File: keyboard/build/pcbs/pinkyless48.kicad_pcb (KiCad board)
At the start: 2 copper layers, 136.1 x 162.6 mm, 49 parts

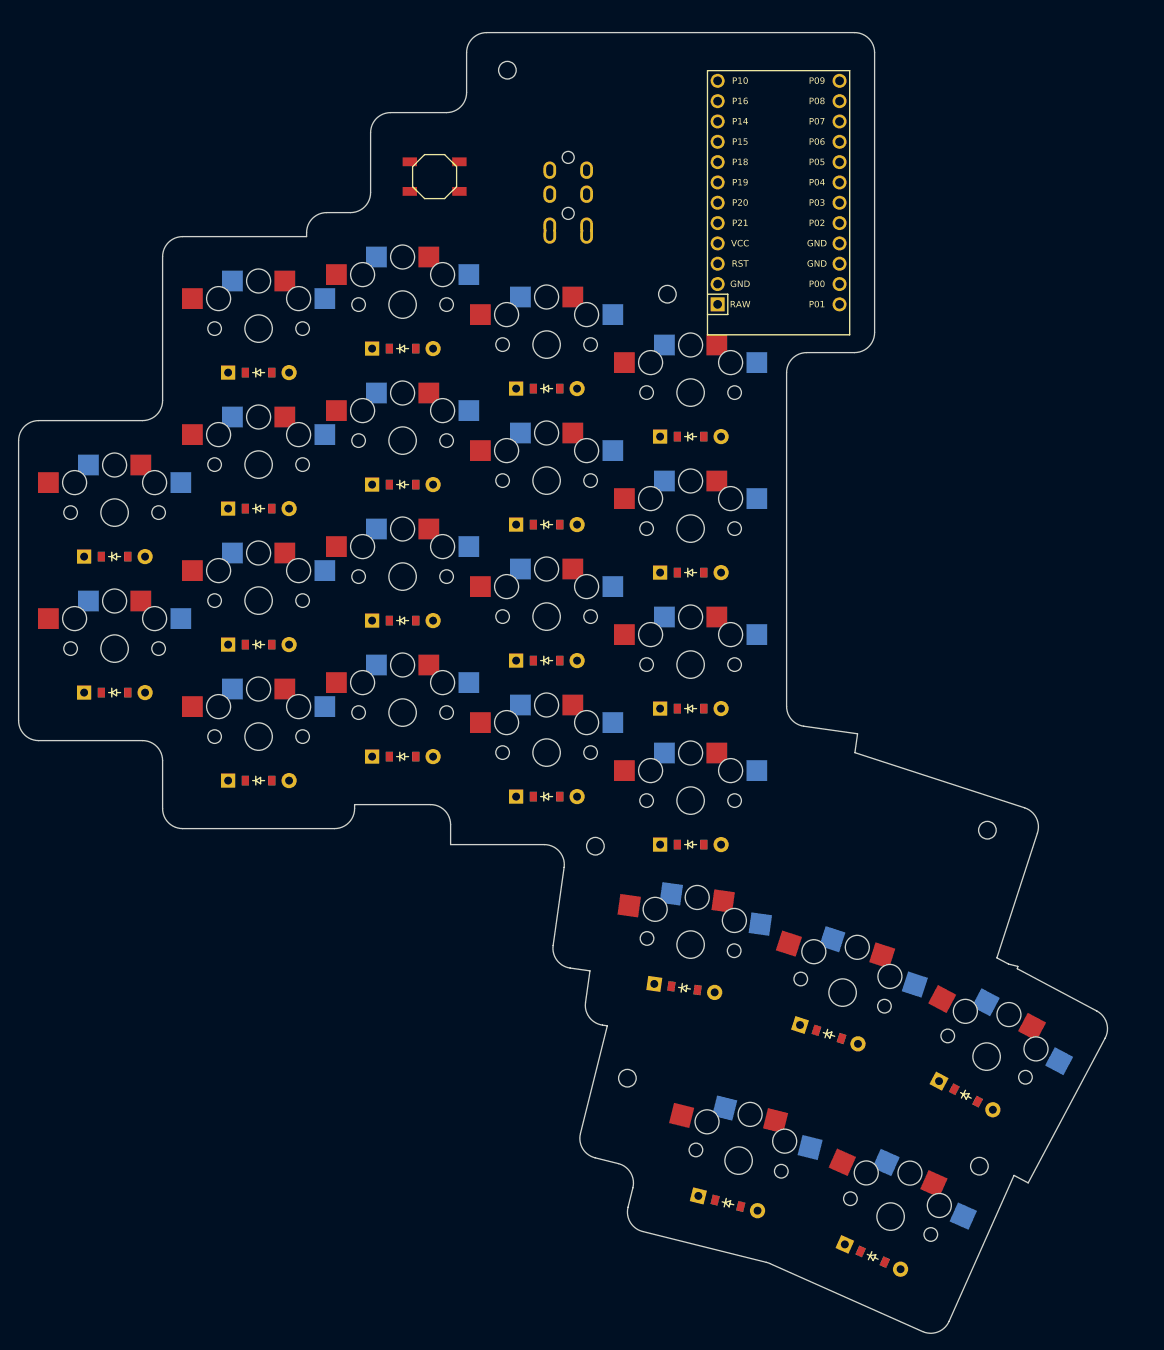
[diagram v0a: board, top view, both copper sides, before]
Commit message: Add pinky number key, flatten stagger, tighten board outline
Three changes, renaming the board to pinkyless48.

Pinky gains a third key. It now drops only the bottom row, keeping number,
top and home. With all five columns present the number row carries a full
1234567890 across the two halves, so digits no longer need a layer. 24 keys
per half, 24 of 25 matrix cells used.

Column stagger reworked to a flat profile: inner, index and ring level with
each other, middle 4 mm forward, pinky 6 mm back. This is not the usual
finger-length stagger.

That change exposed a real constraint. The reversible Choc hotswap footprint
carries socket pads for BOTH faces and is +/-9.58 mm wide, so two columns at
the same height short against each other at an 18 mm pitch - index and inner
are now level and overlapped by 2.99 mm^2. Clearing it needs either 19.4 mm
of pitch or 2.9 mm of vertical offset. Rather than widen every column, only
the inner column's pitch opens to 19.8 mm; every other gap stays at 18 mm and
clears on vertical offset alone. Tightest different-net gap is now 0.650 mm.

Board outline tightened. The two large bridge rectangles are gone: they dated
from when the thumb cluster sat far below the matrix, and now that it starts
at the inner column its key pads already overlap their neighbours. A single
small web patch covers the one gap the thumb keys leave between them. The
reset button moves in beside the controller instead of sitting far outboard,
and the jack pad narrows from 30 to 16 mm, removing the wide slab of empty
board across the top.

Also fixes a genuine bug in find_mounts.py: the reference anchor was
hardcoded at matrix_pinky_home's old coordinates, so once the stagger moved
that key every emitted screw position was offset by 6 mm. It now reads the
anchor from the build.

Case STLs, QMK keyboard.json and the keymap regenerated for 48 keys. All five
checks pass.

Co-Authored-By: Claude Opus 5 <noreply@anthropic.com>
Claude-Session: https://claude.ai/code/sess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
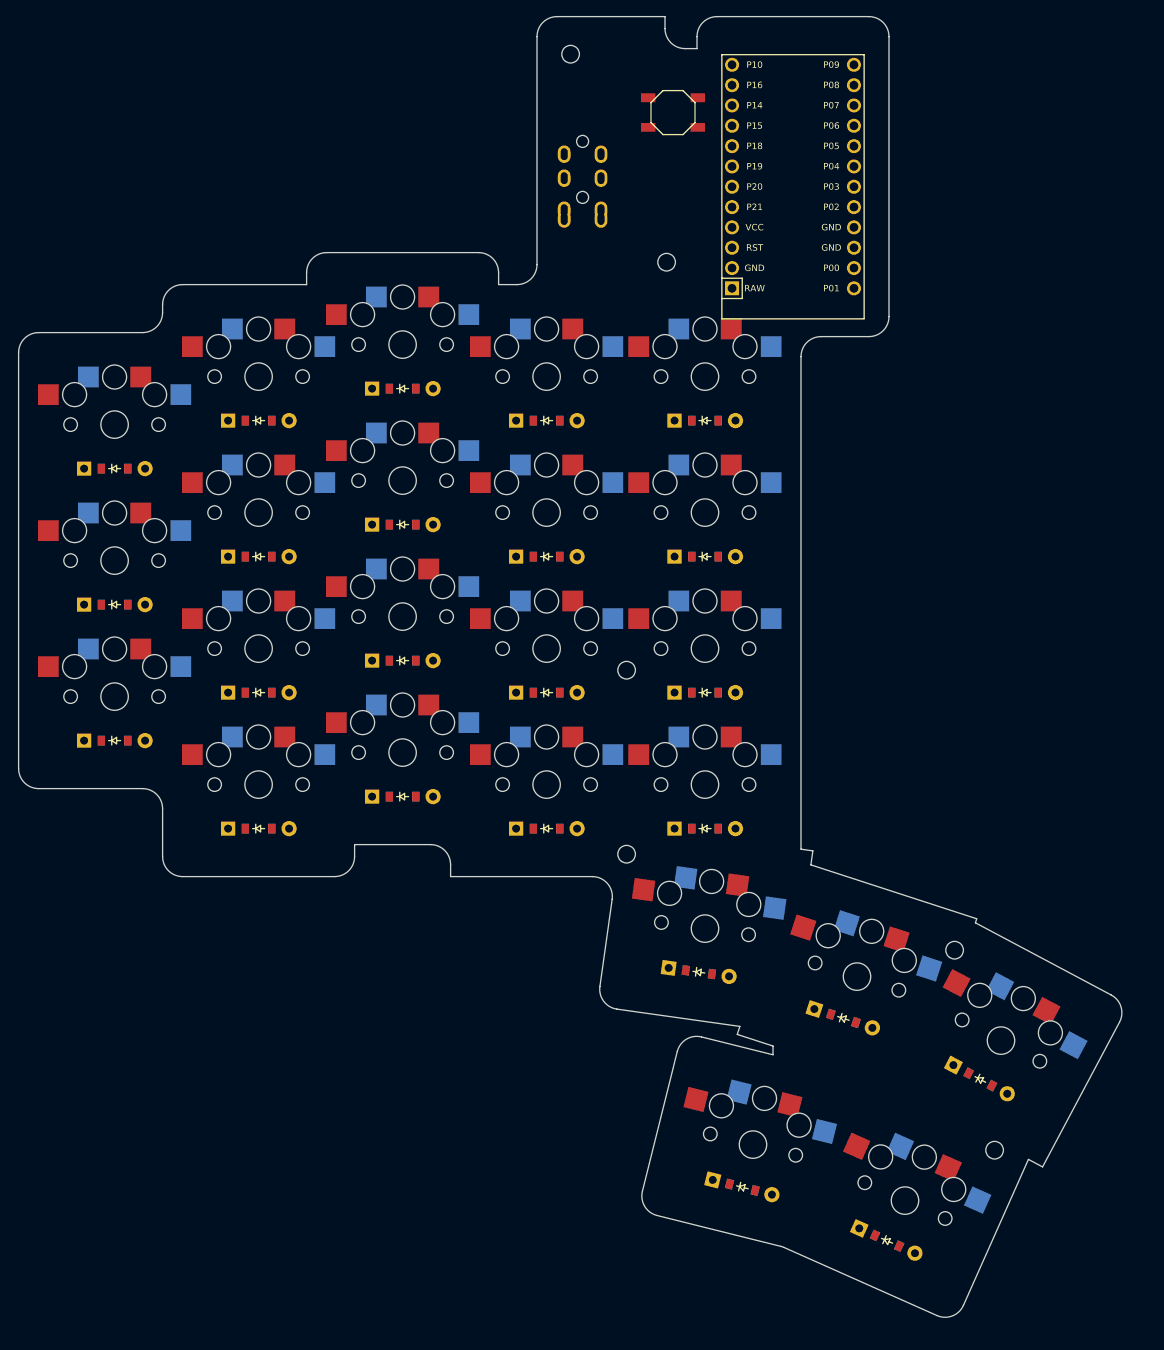
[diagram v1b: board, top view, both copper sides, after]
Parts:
- added D24: , ComboDiode, F.Cu at (156.6, 217.0)
- added S24: , PG1350, F.Cu at (158.8, 212.0)
- moved S19 71.0 mm to (133.8, 109.0), turned to 0 degrees
- moved D19 71.0 mm to (133.8, 114.5), turned to 0 degrees
- moved D15 56.0 mm to (114.0, 114.5)
- moved S15 56.0 mm to (114.0, 109.0)
- moved D11 54.1 mm to (96.0, 110.5)
- moved S11 54.1 mm to (96.0, 105.0)
- moved D7 45.7 mm to (78.0, 114.5)
- moved S7 45.7 mm to (78.0, 109.0)
- moved D3 43.0 mm to (60.0, 120.5)
- moved S3 43.0 mm to (60.0, 115.0)
- moved S22 36.1 mm to (170.8, 192.0), turned to -28 degrees
- moved D22 35.1 mm to (168.2, 196.9), turned to -28 degrees
- moved B1 30.9 mm to (129.8, 76.0)
- moved D4 23.0 mm to (78.0, 165.5)
- moved D5 23.0 mm to (78.0, 148.5)
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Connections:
- D10 pad 1: R4 -> R3
- D10 pad 2: middle_num -> middle_top
- D11 pad 1: R1 -> R4
- D11 pad 2: index_bottom -> middle_num
- D12 pad 1: R2 -> R1
- D12 pad 2: index_home -> index_bottom
- D13 pad 1: R3 -> R2
- D13 pad 2: index_top -> index_home
- D14 pad 1: R4 -> R3
- D14 pad 2: index_num -> index_top
- D15 pad 1: R1 -> R4
- D15 pad 2: inner_bottom -> index_num
- D16 pad 1: R2 -> R1
- D16 pad 2: inner_home -> inner_bottom
- D17 pad 1: R3 -> R2
- D17 pad 2: inner_top -> inner_home
- D18 pad 1: R4 -> R3
- D18 pad 2: inner_num -> inner_top
- D19 pad 1: R5 -> R4
- D19 pad 2: t1_thumb -> inner_num
- D20 pad 2: t2_thumb -> t1_thumb
- D21 pad 2: t3_thumb -> t2_thumb
- D22 pad 2: t4_thumb -> t3_thumb
- D23 pad 2: t5_thumb -> t4_thumb
- D3 pad 1: R1 -> R4
- D3 pad 2: ring_bottom -> pinky_num
- D4 pad 1: R2 -> R1
- D4 pad 2: ring_home -> ring_bottom
- D5 pad 1: R3 -> R2
- D5 pad 2: ring_top -> ring_home
- D6 pad 1: R4 -> R3
- D6 pad 2: ring_num -> ring_top
- D7 pad 1: R1 -> R4
- D7 pad 2: middle_bottom -> ring_num
- D8 pad 1: R2 -> R1
- D8 pad 2: middle_home -> middle_bottom
- D9 pad 1: R3 -> R2
- D9 pad 2: middle_top -> middle_home
- S10 pad 1: middle_num -> middle_top
- S11 pad 1: index_bottom -> middle_num
- S11 pad 2: C4 -> C3
- S12 pad 1: index_home -> index_bottom
- S13 pad 1: index_top -> index_home
- S14 pad 1: index_num -> index_top
- S15 pad 1: inner_bottom -> index_num
- S15 pad 2: C5 -> C4
- S16 pad 1: inner_home -> inner_bottom
- S17 pad 1: inner_top -> inner_home
- S18 pad 1: inner_num -> inner_top
- S19 pad 1: t1_thumb -> inner_num
- S19 pad 2: C1 -> C5
- S20 pad 1: t2_thumb -> t1_thumb
- S20 pad 2: C2 -> C1
- S21 pad 1: t3_thumb -> t2_thumb
- S21 pad 2: C3 -> C2
- S22 pad 1: t4_thumb -> t3_thumb
- S22 pad 2: C4 -> C3
- S23 pad 1: t5_thumb -> t4_thumb
- S23 pad 2: C5 -> C4
- S3 pad 1: ring_bottom -> pinky_num
- S3 pad 2: C2 -> C1
- S4 pad 1: ring_home -> ring_bottom
- S5 pad 1: ring_top -> ring_home
- S6 pad 1: ring_num -> ring_top
- S7 pad 1: middle_bottom -> ring_num
- S7 pad 2: C3 -> C2
- S8 pad 1: middle_home -> middle_bottom
- S9 pad 1: middle_top -> middle_home
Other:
- board size 136.1 x 162.6 mm -> 137.9 x 162.6 mm

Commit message: Move controller into the notch beside the thumb cluster
The strip of board above the matrix was 29.5 mm tall and 41% empty. It
existed only because the controller was mounted standing on end: a Pro Micro
is 33 x 18 mm, so vertically it forced the board ~30 mm taller than the
tallest key just to clear it.

Because the thumb cluster runs inboard and down, the area outboard of it and
below the number row is dead space that already sits inside the board's
bounding box. The controller, TRRS jack and reset button now live there, laid
flat with the USB port facing inboard so the cable exits between the halves.
Filling that notch costs nothing in overall size, and the strip above the
matrix disappears entirely.

Board drops from 137.9 x 162.6 mm to 137.9 x 133.1 mm per half - 29.5 mm
shorter, an 18% smaller bounding box, which is also what JLCPCB charges by.

The three separate connector pads collapse into one pad covering the whole
controller area, since the jack and reset button now sit inside it.

Screw positions re-derived. Case STLs, QMK keyboard.json and previews
regenerated. All five checks pass; controller opening now clears the nearest
switch cutout by 3.90 mm, up from 2.05 mm.

Co-Authored-By: Claude Opus 5 <noreply@anthropic.com>
Claude-Session: https://claude.ai/code/session_01TKXtddA7pBLooPYbDwxvxo
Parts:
- moved MCU1 49.0 mm to (161.8, 130.0), turned to 180 degrees
- moved TRRS1 48.5 mm to (161.8, 104.0)
- moved B1 34.4 mm to (149.8, 104.0)
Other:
- board size 137.9 x 162.6 mm -> 137.9 x 133.1 mm

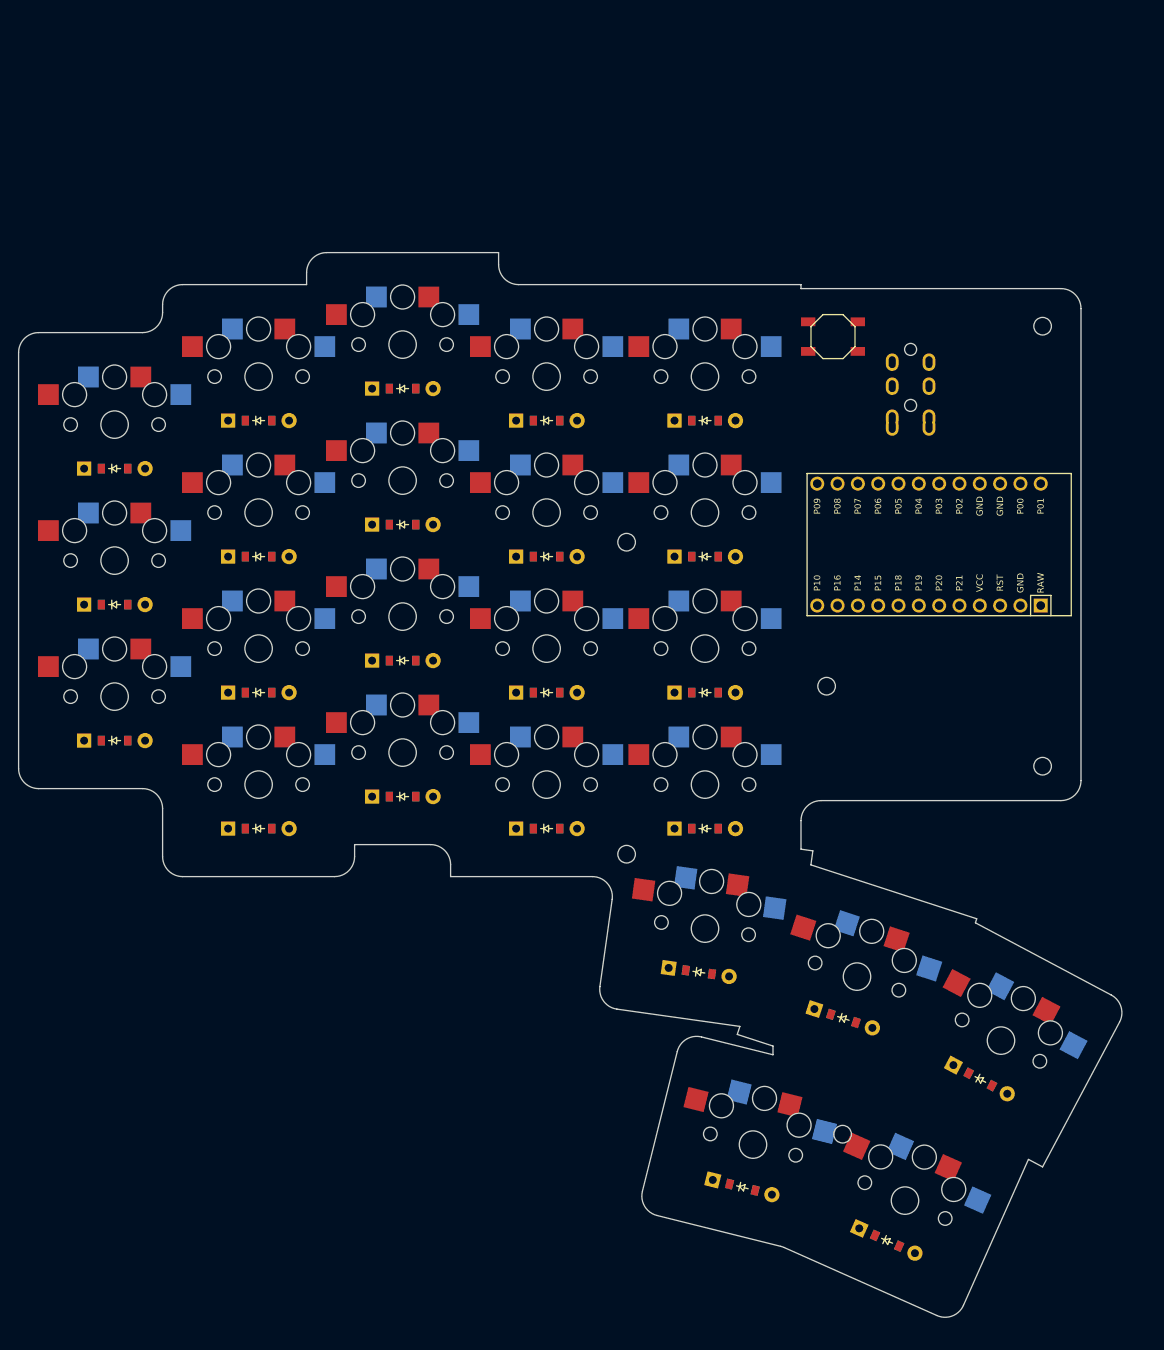
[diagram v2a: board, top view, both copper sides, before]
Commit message: Fill concave notches in the board outline
The outline had ten concave pockets where the thumb cluster, the controller
area and the grown key pads met. They are dead space, and their sharp inside
corners are crack initiation points in both 1.6 mm FR4 and the 1.3 mm printed
plate.

The outline is now morphologically closed - grown by 6 mm, then shrunk by the
same 6 mm - before filleting. That fills any pocket narrower than roughly
12 mm while leaving the board's overall L-shape alone. A convex hull was the
obvious alternative and is wrong here: it would swallow the entire empty
region outboard of the thumb cluster and add roughly 40 cm^2 of pointless
board.

Measured effect: pockets 10 -> 1 (the survivor is a 2 mm^2 sliver), board area
116.0 -> 117.7 cm^2 (+1.5%), bounding box unchanged at 137.9 x 133.1 mm.

Worth recording that the fragility concern did not hold up on measurement:
eroding the outline until it splits showed the narrowest neck was already
22.2 mm, not thin enough to snap. The closing was still worth doing for the
stress risers and the simpler plate, and it takes the neck to 33.0 mm.

check_outline.py now measures both properties on every build - narrowest neck
(fails under 8 mm) and any remaining concave pocket over 100 mm^2 - so a
future layout change cannot quietly reintroduce a fragile outline.

Case STLs, QMK keyboard.json and previews regenerated. All five checks pass.

Co-Authored-By: Claude Opus 5 <noreply@anthropic.com>
Claude-Session: https://claude.ai/code/session_01TKXtddA7pBLooPYbDwxvxo
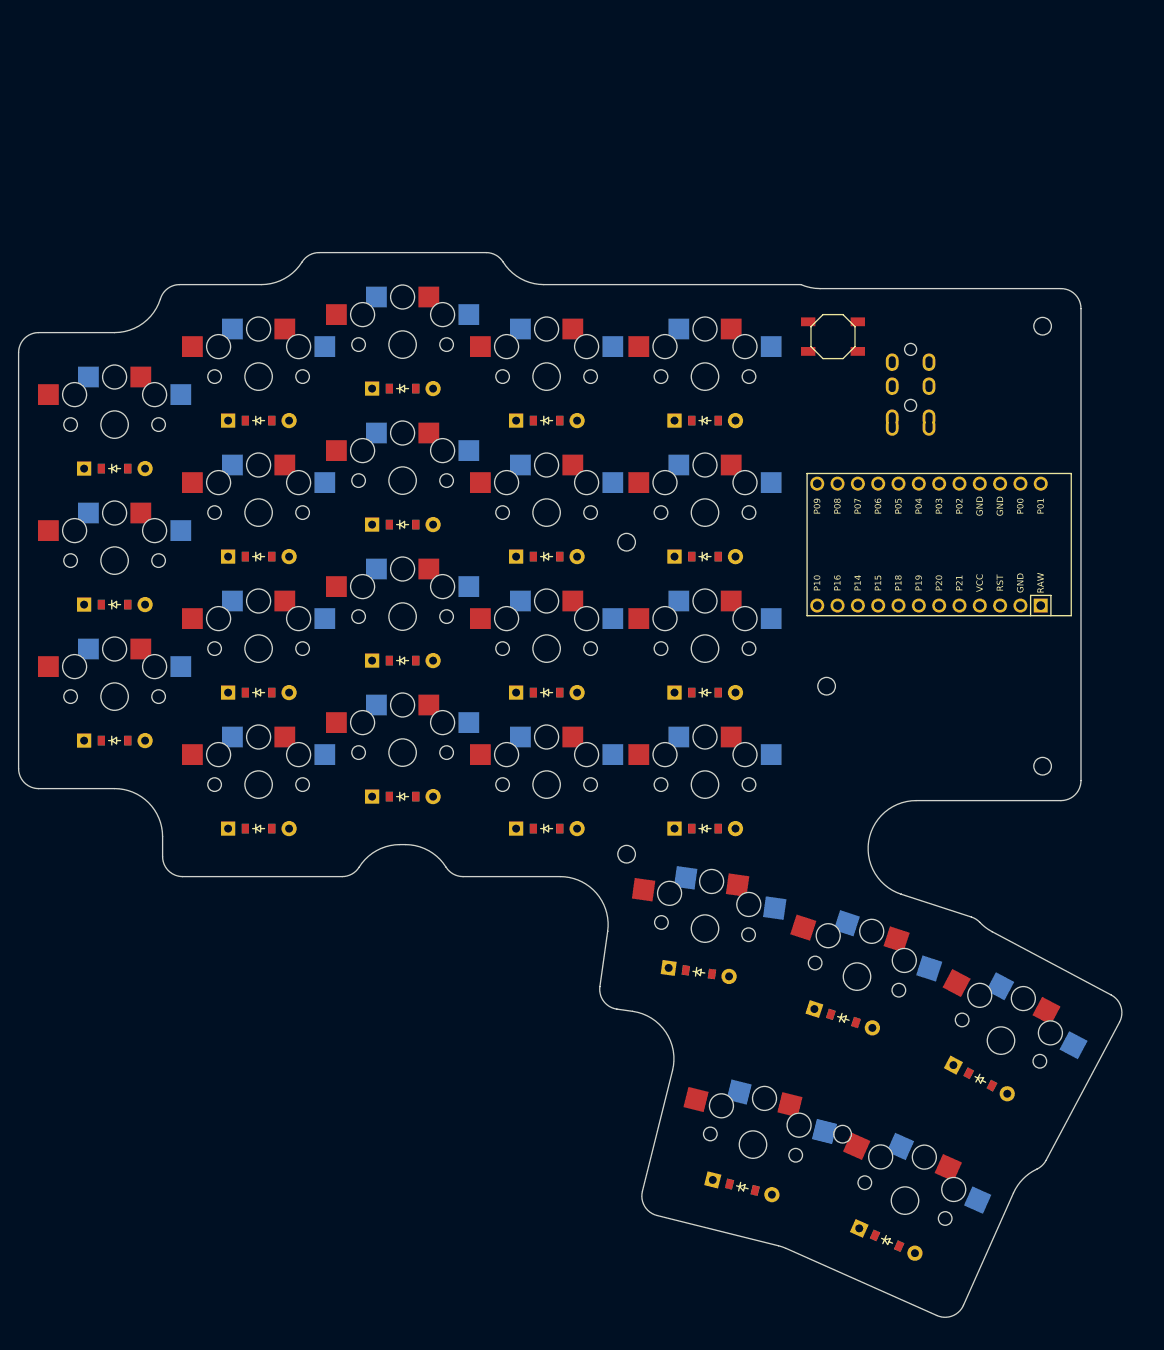
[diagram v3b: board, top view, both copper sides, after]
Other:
- outline, holes or cut-outs redrawn
